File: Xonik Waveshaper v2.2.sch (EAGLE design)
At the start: 92 parts, among them IC1 TL074D, IC2 TL074D, IC3 TL074D, IC4 TL072D, IC5 4013D, IC6 LM311D, T1 2n3904

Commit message: Reduced footprints for op amps
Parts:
- added C15, C17, C18, C19: 1uF, rcl:C-EUC0402
- IC1, IC2, IC3: value TL074D -> TL074JT; device linear:TL074D -> joakim:TL074JT
- IC6: value LM311D -> LM311T; device linear:LM311D -> joakim:LM311T
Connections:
- net N$20 renamed SS2_TRIM_R
- net N$23 renamed SS1_TRIM_L
- net N$28 renamed SS2_TRIM_L
- net N$33 renamed PW_CV
- net N$41 renamed SS1_TRIM_R
- net +12V: now also C15.2, C18.2
- net -12V: now also C17.1, C19.1
- net GND: now also C15.1, C17.2, C18.1, C19.2
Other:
- note removed: "TODO: kan vi ha dedikert clean 5V?"
- moved on the sheet: C10, C11, C12, C9, IC1A, IC1B, IC1C, IC1D, IC2A, IC2B, IC2C, IC2D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

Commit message: Almost all tracing done!
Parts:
- 22: device resistor:R-EU_R0805 -> rcl:R-EU_R0603
- C1, C14, C2, C3, C4, C5, C6, C7: device rcl:C-EUC0603 -> joakim:C-EU-J0603
- IC4: value TL072D -> TL072JT; device joakim:TL072D -> joakim:TL072JT
- IC5: value 4013D -> 4013T; device joakim:4013D -> joakim:4013T
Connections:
- net GND: now also IC1B.+IN; no longer IC1A.+IN
- net INV_SAW: now also IC1B.OUT; no longer IC1A.OUT
- net N$1: now also IC2A.-IN; no longer IC2B.-IN
- net N$10: now also IC1B.-IN; no longer IC1A.-IN
- net N$15: now also IC2B.-IN; no longer IC2A.-IN
- net N$42: now also IC2A.OUT; no longer IC2B.OUT
- net N$5: now also IC1A.+IN; no longer IC1B.+IN
- net N$6: now also IC1A.-IN; no longer IC1B.-IN
- net PULSE: now also IC1A.OUT; no longer IC1B.OUT
- net SAW: now also IC2B.OUT; no longer IC2A.OUT
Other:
- moved on the sheet: IC1A, IC1B, IC2A, IC2B, IC4A, IC4B

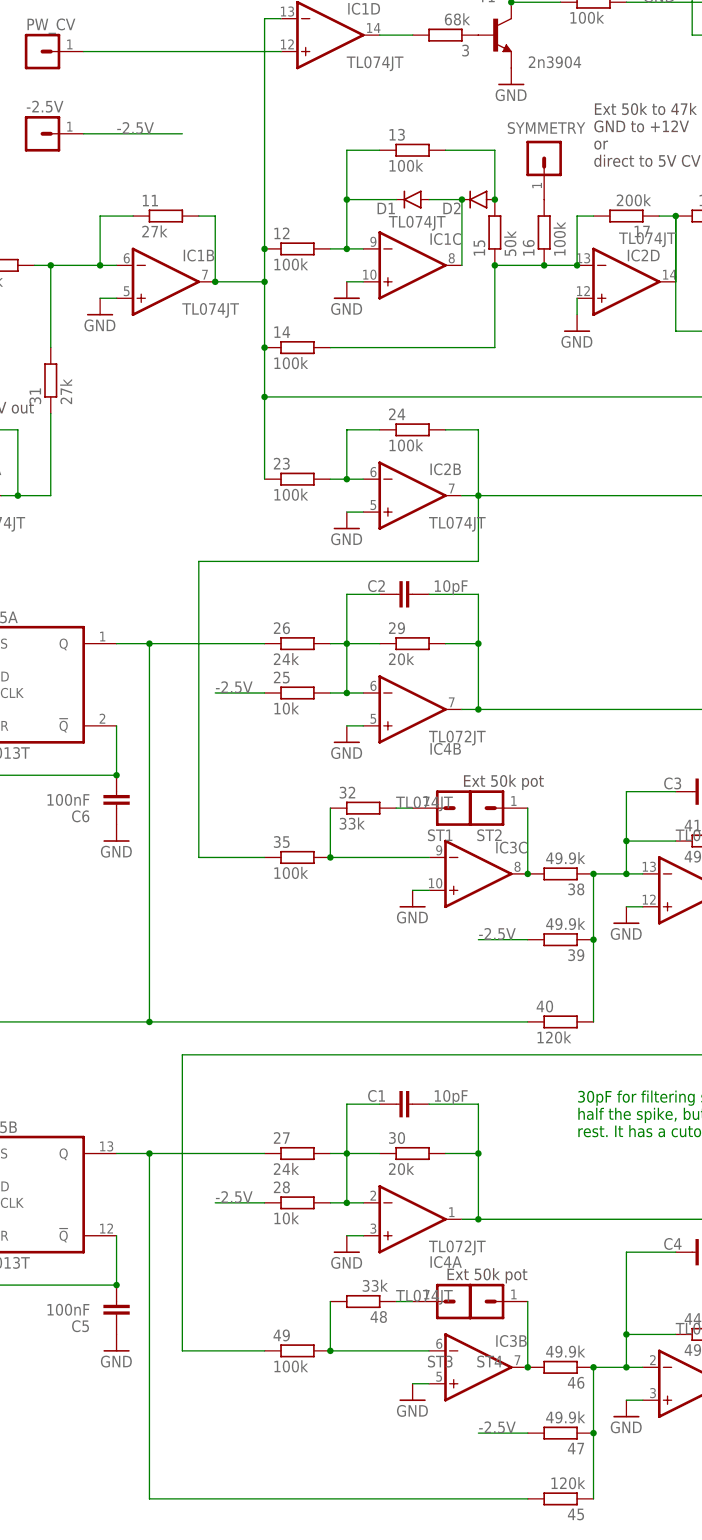
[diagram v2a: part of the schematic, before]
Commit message: Changed waveshaper to -5V
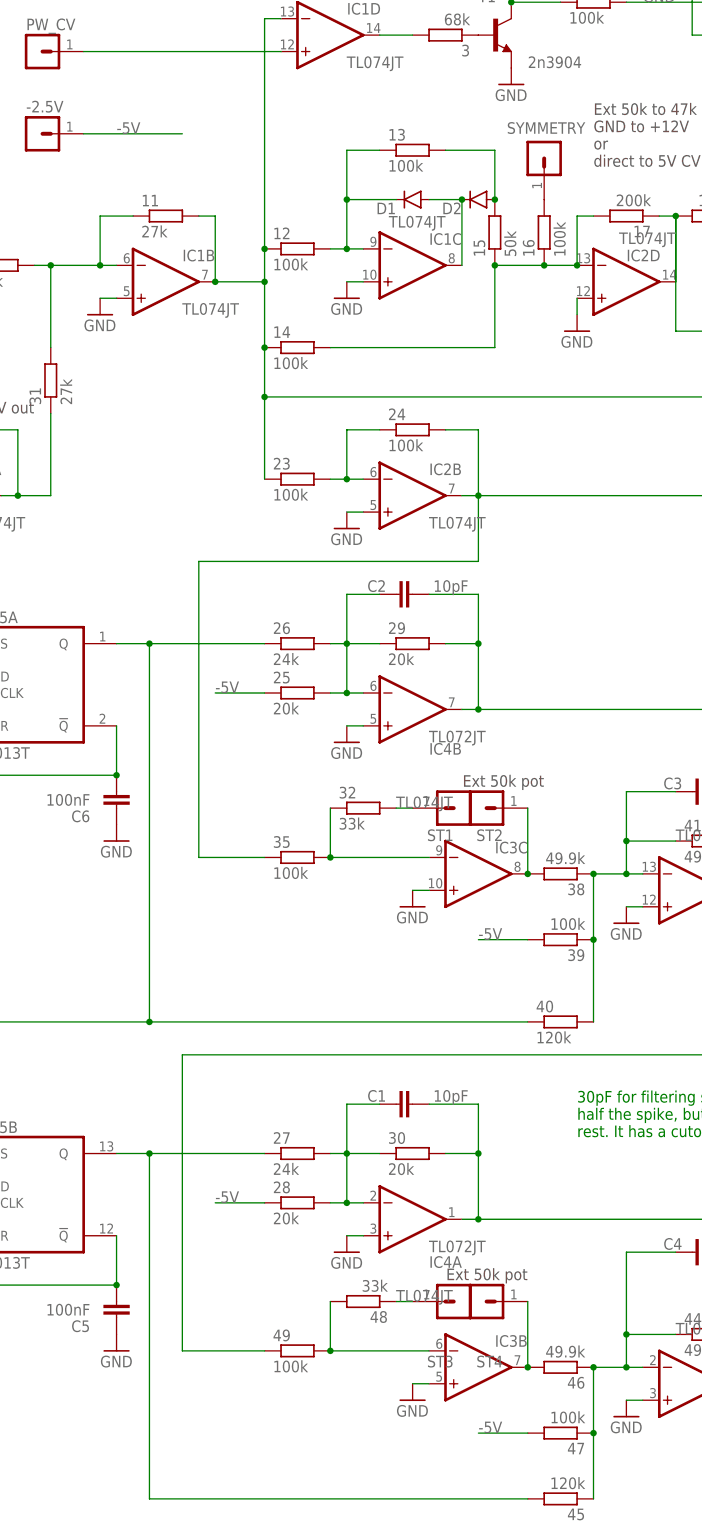
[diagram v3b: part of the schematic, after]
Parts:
- 25, 28: value 10k -> 20k
- 39, 47: value 49.9k -> 100k
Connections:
- net -2.5V renamed -5V
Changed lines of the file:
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@@
 <part name="24" library="rcl" library_urn="urn:adsk.eagle:library:334" deviceset="R-EU_" device="R0603" package3d_urn="urn:adsk.eagle:package:23555/3" value="100k"/>
 <part name="GND5" library="supply1" deviceset="GND" device=""/>
-<part name="25" library="rcl" library_urn="urn:adsk.eagle:library:334" deviceset="R-EU_" device="R0603" package3d_urn="urn:adsk.eagle:package:23555/3" value="10k"/>
+<part name="25" library="rcl" library_urn="urn:adsk.eagle:library:334" deviceset="R-EU_" device="R0603" package3d_urn="urn:adsk.eagle:package:23555/3" value="20k"/>
 <part name="26" library="rcl" library_urn="urn:adsk.eagle:library:334" deviceset="R-EU_" device="R0603" package3d_urn="urn:adsk.eagle:package:23555/3" value="24k"/>
 <part name="27" library="rcl" library_urn="urn:adsk.eagle:library:334" deviceset="R-EU_" device="R0603" package3d_urn="urn:adsk.eagle:package:23555/3" value="24k"/>
-<part name="28" library="rcl" library_urn="urn:adsk.eagle:library:334" deviceset="R-EU_" device="R0603" package3d_urn="urn:adsk.eagle:package:23555/3" value="10k"/>
+<part name="28" library="rcl" library_urn="urn:adsk.eagle:library:334" deviceset="R-EU_" device="R0603" package3d_urn="urn:adsk.eagle:package:23555/3" value="20k"/>
 <part name="29" library="rcl" library_urn="urn:adsk.eagle:library:334" deviceset="R-EU_" device="R0603" package3d_urn="urn:adsk.eagle:package:23555/3" value="20k"/>
 <part name="30" library="rcl" library_urn="urn:adsk.eagle:library:334" deviceset="R-EU_" device="R0603" package3d_urn="urn:adsk.eagle:package:23555/3" value="20k"/>
@@
 <part name="GND8" library="supply1" deviceset="GND" device=""/>
 <part name="38" library="rcl" library_urn="urn:adsk.eagle:library:334" deviceset="R-EU_" device="R0603" package3d_urn="urn:adsk.eagle:package:23555/3" value="49.9k"/>
-<part name="39" library="rcl" library_urn="urn:adsk.eagle:library:334" deviceset="R-EU_" device="R0603" package3d_urn="urn:adsk.eagle:package:23555/3" value="49.9k"/>
+<part name="39" library="rcl" library_urn="urn:adsk.eagle:library:334" deviceset="R-EU_" device="R0603" package3d_urn="urn:adsk.eagle:package:23555/3" value="100k"/>
 <part name="40" library="rcl" library_urn="urn:adsk.eagle:library:334" deviceset="R-EU_" device="R0603" package3d_urn="urn:adsk.eagle:package:23555/3" value="120k"/>
 <part name="41" library="rcl" library_urn="urn:adsk.eagle:library:334" deviceset="R-EU_" device="R0603" package3d_urn="urn:adsk.eagle:package:23555/3" value="49.9k"/>
@@
 <part name="45" library="rcl" library_urn="urn:adsk.eagle:library:334" deviceset="R-EU_" device="R0603" package3d_urn="urn:adsk.eagle:package:23555/3" value="120k"/>
 <part name="46" library="rcl" library_urn="urn:adsk.eagle:library:334" deviceset="R-EU_" device="R0603" package3d_urn="urn:adsk.eagle:package:23555/3" value="49.9k"/>
-<part name="47" library="rcl" library_urn="urn:adsk.eagle:library:334" deviceset="R-EU_" device="R0603" package3d_urn="urn:adsk.eagle:package:23555/3" value="49.9k"/>
+<part name="47" library="rcl" library_urn="urn:adsk.eagle:library:334" deviceset="R-EU_" device="R0603" package3d_urn="urn:adsk.eagle:package:23555/3" value="100k"/>
 <part name="48" library="rcl" library_urn="urn:adsk.eagle:library:334" deviceset="R-EU_" device="R0603" package3d_urn="urn:adsk.eagle:package:23555/3" value="33k"/>
 <part name="49" library="rcl" library_urn="urn:adsk.eagle:library:334" deviceset="R-EU_" device="R0603" package3d_urn="urn:adsk.eagle:package:23555/3" value="100k"/>
@@
 </segment>
 </net>
-<net name="-2.5V" class="0">
+<net name="-5V" class="0">
 <segment>
 <pinref part="25" gate="G$1" pin="1"/>

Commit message: Changed pins to smaller ones
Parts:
- +12V, -12V, -2.5V, DCO_IN, GND, INV_SAW, IN_CENTER, PULSE, PULSE_AMP_CV, PW_CV, SAW, SINE, ST1, ST2, ST3, ST4, SUB_SAW_1, SUB_SAW_2, SUB_SQR_1, SUB_SQR_2, SYMMETRY, TRIANGLE: device joakim:MA01-1JP -> joakim:MA01-1JN
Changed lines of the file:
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@@
 <part name="C11" library="rcl" library_urn="urn:adsk.eagle:library:334" deviceset="C-EU" device="C0402" package3d_urn="urn:adsk.eagle:package:23626/2" value="1uF"/>
 <part name="C8" library="rcl" library_urn="urn:adsk.eagle:library:334" deviceset="C-EU" device="C0402" package3d_urn="urn:adsk.eagle:package:23626/2" value="1uF"/>
-<part name="PULSE" library="joakim" deviceset="MA01-1J" device="P"/>
-<part name="SINE" library="joakim" deviceset="MA01-1J" device="P"/>
-<part name="TRIANGLE" library="joakim" deviceset="MA01-1J" device="P"/>
-<part name="INV_SAW" library="joakim" deviceset="MA01-1J" device="P"/>
-<part name="SAW" library="joakim" deviceset="MA01-1J" device="P"/>
-<part name="SUB_SQR_1" library="joakim" deviceset="MA01-1J" device="P"/>
-<part name="SUB_SAW_1" library="joakim" deviceset="MA01-1J" device="P"/>
-<part name="SUB_SQR_2" library="joakim" deviceset="MA01-1J" device="P"/>
-<part name="SUB_SAW_2" library="joakim" deviceset="MA01-1J" device="P"/>
-<part name="PULSE_AMP_CV" library="joakim" deviceset="MA01-1J" device="P"/>
-<part name="PW_CV" library="joakim" deviceset="MA01-1J" device="P"/>
-<part name="DCO_IN" library="joakim" deviceset="MA01-1J" device="P"/>
-<part name="+12V" library="joakim" deviceset="MA01-1J" device="P"/>
-<part name="GND" library="joakim" deviceset="MA01-1J" device="P"/>
-<part name="-12V" library="joakim" deviceset="MA01-1J" device="P"/>
-<part name="IN_CENTER" library="joakim" deviceset="MA01-1J" device="P"/>
-<part name="SYMMETRY" library="joakim" deviceset="MA01-1J" device="P"/>
-<part name="ST1" library="joakim" deviceset="MA01-1J" device="P"/>
-<part name="ST2" library="joakim" deviceset="MA01-1J" device="P"/>
-<part name="ST3" library="joakim" deviceset="MA01-1J" device="P"/>
-<part name="ST4" library="joakim" deviceset="MA01-1J" device="P"/>
+<part name="PULSE" library="joakim" deviceset="MA01-1J" device="N"/>
+<part name="SINE" library="joakim" deviceset="MA01-1J" device="N"/>
+<part name="TRIANGLE" library="joakim" deviceset="MA01-1J" device="N"/>
+<part name="INV_SAW" library="joakim" deviceset="MA01-1J" device="N"/>
+<part name="SAW" library="joakim" deviceset="MA01-1J" device="N"/>
+<part name="SUB_SQR_1" library="joakim" deviceset="MA01-1J" device="N"/>
+<part name="SUB_SAW_1" library="joakim" deviceset="MA01-1J" device="N"/>
+<part name="SUB_SQR_2" library="joakim" deviceset="MA01-1J" device="N"/>
+<part name="SUB_SAW_2" library="joakim" deviceset="MA01-1J" device="N"/>
+<part name="PULSE_AMP_CV" library="joakim" deviceset="MA01-1J" device="N"/>
+<part name="PW_CV" library="joakim" deviceset="MA01-1J" device="N"/>
+<part name="DCO_IN" library="joakim" deviceset="MA01-1J" device="N"/>
+<part name="+12V" library="joakim" deviceset="MA01-1J" device="N"/>
+<part name="GND" library="joakim" deviceset="MA01-1J" device="N"/>
+<part name="-12V" library="joakim" deviceset="MA01-1J" device="N"/>
+<part name="IN_CENTER" library="joakim" deviceset="MA01-1J" device="N"/>
+<part name="SYMMETRY" library="joakim" deviceset="MA01-1J" device="N"/>
+<part name="ST1" library="joakim" deviceset="MA01-1J" device="N"/>
+<part name="ST2" library="joakim" deviceset="MA01-1J" device="N"/>
+<part name="ST3" library="joakim" deviceset="MA01-1J" device="N"/>
+<part name="ST4" library="joakim" deviceset="MA01-1J" device="N"/>
 <part name="GND26" library="supply1" deviceset="GND" device=""/>
 <part name="GND28" library="supply1" deviceset="GND" device=""/>
@@
 <part name="SUPPLY10" library="supply2" library_urn="urn:adsk.eagle:library:372" deviceset="+12V" device=""/>
 <part name="SUPPLY11" library="supply2" library_urn="urn:adsk.eagle:library:372" deviceset="-12V" device=""/>
-<part name="-2.5V" library="joakim" deviceset="MA01-1J" device="P"/>
+<part name="-2.5V" library="joakim" deviceset="MA01-1J" device="N"/>
 <part name="GND1" library="supply1" deviceset="GND" device=""/>
 <part name="9" library="rcl" library_urn="urn:adsk.eagle:library:334" deviceset="R-EU_" device="R0603" package3d_urn="urn:adsk.eagle:package:23555/3" value="30k"/>

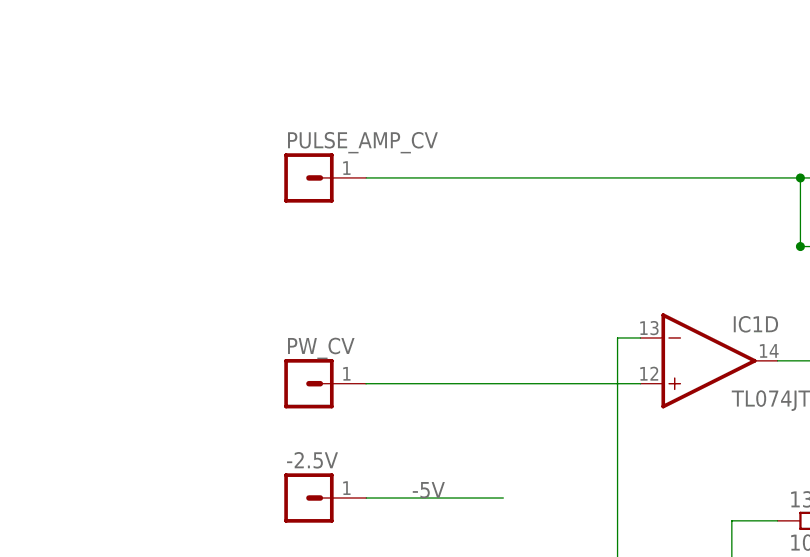
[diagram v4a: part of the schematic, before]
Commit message: Comment about bipolar PWM
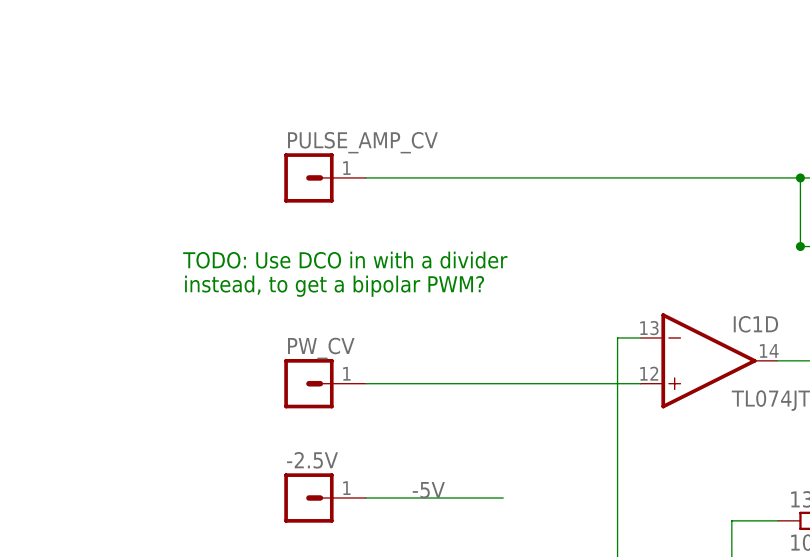
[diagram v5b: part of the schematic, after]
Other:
- note added: "TODO: Use DCO in with a divider instead, to get a bipolar PWM?"
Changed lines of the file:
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@@
 here? Not sure.</text>
 <text x="-154.94" y="-43.18" size="5.08" layer="91">TODO: Replace with TSSOP08</text>
+<text x="-48.26" y="91.44" size="1.778" layer="91">TODO: Use DCO in with a divider
+instead, to get a bipolar PWM?</text>
 </plain>
 <instances>
